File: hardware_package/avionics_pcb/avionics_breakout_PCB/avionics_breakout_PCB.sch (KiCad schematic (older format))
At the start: 15 parts, among them J0 GPS, J1 ANT, J2 SER_1, J3 SER_2, J4 IGN_1, J5 IGN_2, J6 IGN_3, J7 IGN_4, J8 3V3_IN, J9 GND_IN, SW1 SW_Push

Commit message: Finished the new PCB layout for the breakout avionics PCB
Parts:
- Barometer1: symbol avionics_breakout_PCB-rescue:MPL3115A2-Adafruit-avionics -> avionics:MPL3115A2-Adafruit
- IMU1: symbol avionics_breakout_PCB-rescue:MPU-6050-Adafruit-avionics -> avionics:MPU-6050-Adafruit
- LoRa_Radio1: symbol avionics_breakout_PCB-rescue:RFM98-avionics -> avionics:RFM98
- STM32: symbol avionics_breakout_PCB-rescue:Adafruit_Feather_STM32F405-avionics -> avionics:Adafruit_Feather_STM32F405
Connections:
- net +3V3: now also LoRa_Radio1.13 (3V3); no longer LoRa_Radio1.5 (3V3)
- net CS: now also LoRa_Radio1.5 (NSS); no longer LoRa_Radio1.12 (NSS)
- net GND: now also LoRa_Radio1.1 (GND), LoRa_Radio1.10 (GND), LoRa_Radio1.8 (GND); no longer LoRa_Radio1.16 (GND), LoRa_Radio1.2 (GND), LoRa_Radio1.9 (GND)
- net INT_LORA: now also LoRa_Radio1.14 (DIO0); no longer LoRa_Radio1.6 (DIO0)
- net MISO: now also LoRa_Radio1.2 (MISO); no longer LoRa_Radio1.15 (MISO)
- net MOSI: now also LoRa_Radio1.3 (MOSI); no longer LoRa_Radio1.14 (MOSI)
- net RESET: now also LoRa_Radio1.6 (RESET); no longer LoRa_Radio1.11 (RESET)
- net SCK: now also LoRa_Radio1.4 (SCK); no longer LoRa_Radio1.13 (SCK)
- net at J1.1 (Pin_1): now also LoRa_Radio1.9 (ANT); no longer LoRa_Radio1.1 (ANT)
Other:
- moved on the sheet: J1, LoRa_Radio1
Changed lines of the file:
@@
 Text GLabel 6800 1400 0    50   Input ~ 0
 SDA
-Text GLabel 7050 2600 0    50   Input ~ 0
+Text GLabel 7000 2750 0    50   Input ~ 0
 RESET
-Text GLabel 7050 2200 0    50   Input ~ 0
+Text GLabel 7000 2350 0    50   Input ~ 0
 MISO
-Text GLabel 7050 2300 0    50   Input ~ 0
+Text GLabel 7000 2450 0    50   Input ~ 0
 MOSI
-Text GLabel 7050 2400 0    50   Input ~ 0
+Text GLabel 7000 2550 0    50   Input ~ 0
 SCK
-Text GLabel 7050 2500 0    50   Input ~ 0
+Text GLabel 7000 2650 0    50   Input ~ 0
 CS
 Text GLabel 2950 2300 2    50   Input ~ 0
@@
 L power:GND #PWR0102
 U 1 1 5F641D27
-P 6700 3050
-F 0 "#PWR0102" H 6700 2800 50  0001 C CNN
-F 1 "GND" H 6705 2877 50  0000 C CNN
-F 2 "" H 6700 3050 50  0001 C CNN
-F 3 "" H 6700 3050 50  0001 C CNN
-	1    6700 3050
+P 6650 3200
+F 0 "#PWR0102" H 6650 2950 50  0001 C CNN
+F 1 "GND" H 6655 3027 50  0000 C CNN
+F 2 "" H 6650 3200 50  0001 C CNN
+F 3 "" H 6650 3200 50  0001 C CNN
+	1    6650 3200
 	1    0    0    -1
 $EndComp
@@
 	7000 4100 7000 4150
 Wire Wire Line
-	8050 2700 8200 2700
-Wire Wire Line
-	8200 2700 8200 3050
-$Comp
-L avionics_breakout_PCB-rescue:RFM98-avionics LoRa_Radio1
+	8000 2850 8150 2850
+Wire Wire Line
+	8150 2850 8150 3200
+$Comp
+L avionics:RFM98 LoRa_Radio1
 U 1 1 5F636F5E
-P 7550 2450
-F 0 "LoRa_Radio1" H 7550 3065 50  0000 C CNN
-F 1 "RFM98" H 7550 2974 50  0000 C CNN
-F 2 "avionics:RFM98" H 7550 1900 50  0001 C CNN
-F 3 "" H 7550 2450 50  0001 C CNN
-	1    7550 2450
-	1    0    0    -1
-$EndComp
-Wire Wire Line
-	7050 2100 6700 2100
-Wire Wire Line
-	6700 2100 6700 2800
-Wire Wire Line
-	6700 2800 7050 2800
-Connection ~ 6700 2800
-Wire Wire Line
-	6700 2800 6700 3050
-Wire Wire Line
-	8200 3050 6700 3050
-Connection ~ 6700 3050
-$Comp
-L avionics_breakout_PCB-rescue:MPL3115A2-Adafruit-avionics Barometer1
+P 7500 2600
+F 0 "LoRa_Radio1" H 7500 3215 50  0000 C CNN
+F 1 "RFM98" H 7500 3124 50  0000 C CNN
+F 2 "avionics:RFM98" H 7500 2050 50  0001 C CNN
+F 3 "" H 7500 2600 50  0001 C CNN
+	1    7500 2600
+	1    0    0    -1
+$EndComp
+Wire Wire Line
+	7000 2250 6650 2250
+Wire Wire Line
+	6650 2250 6650 2950
+Wire Wire Line
+	6650 2950 7000 2950
+Connection ~ 6650 2950
+Wire Wire Line
+	6650 2950 6650 3200
+Wire Wire Line
+	8150 3200 6650 3200
+Connection ~ 6650 3200
+$Comp
+L avionics:MPL3115A2-Adafruit Barometer1
 U 1 1 5F6344B6
 P 7350 4700
@@
 NoConn ~ 8300 1300
 NoConn ~ 8300 1400
-NoConn ~ 8050 2100
-NoConn ~ 8050 2200
-NoConn ~ 8050 2500
-NoConn ~ 8050 2600
-NoConn ~ 7050 2700
+NoConn ~ 8000 2250
+NoConn ~ 8000 2350
+NoConn ~ 8000 2650
+NoConn ~ 8000 2750
+NoConn ~ 7000 2850
 NoConn ~ 7250 4200
 NoConn ~ 7250 4300
@@
 $EndComp
 $Comp
-L avionics_breakout_PCB-rescue:MPU-6050-Adafruit-avionics IMU1
+L avionics:MPU-6050-Adafruit IMU1
 U 1 1 5F631A9D
 P 7550 1250
@@
 L power:+3.3V #PWR0110
 U 1 1 5F67048B
-P 8600 2400
-F 0 "#PWR0110" H 8600 2250 50  0001 C CNN
-F 1 "+3.3V" H 8615 2573 50  0000 C CNN
-F 2 "" H 8600 2400 50  0001 C CNN
-F 3 "" H 8600 2400 50  0001 C CNN
-	1    8600 2400
-	1    0    0    -1
-$EndComp
-Wire Wire Line
-	8600 2400 8050 2400
+P 8550 2550
+F 0 "#PWR0110" H 8550 2400 50  0001 C CNN
+F 1 "+3.3V" H 8565 2723 50  0000 C CNN
+F 2 "" H 8550 2550 50  0001 C CNN
+F 3 "" H 8550 2550 50  0001 C CNN
+	1    8550 2550
+	1    0    0    -1
+$EndComp
+Wire Wire Line
+	8550 2550 8000 2550
 $Comp
 L power:+3.3V #PWR0111
@@
 L Connector:Conn_01x01_Male J1
 U 1 1 5F636A13
-P 8550 2800
-F 0 "J1" H 8522 2732 50  0000 R CNN
-F 1 "ANT" H 8522 2823 50  0000 R CNN
-F 2 "Connector_Wire:SolderWire-0.1sqmm_1x01_D0.4mm_OD1mm" H 8550 2800 50  0001 C CNN
-F 3 "~" H 8550 2800 50  0001 C CNN
-	1    8550 2800
-	-1   0    0    1
-$EndComp
-Wire Wire Line
-	8050 2800 8350 2800
-Text GLabel 8050 2300 2    50   Input ~ 0
+P 8500 2950
+F 0 "J1" H 8472 2882 50  0000 R CNN
+F 1 "ANT" H 8472 2973 50  0000 R CNN
+F 2 "Connector_Wire:SolderWire-0.1sqmm_1x01_D0.4mm_OD1mm" H 8500 2950 50  0001 C CNN
+F 3 "~" H 8500 2950 50  0001 C CNN
+	1    8500 2950
+	-1   0    0    1
+$EndComp
+Wire Wire Line
+	8000 2950 8300 2950
+Text GLabel 8000 2450 2    50   Input ~ 0
 INT_LORA
 $Comp
-L avionics_breakout_PCB-rescue:Adafruit_Feather_STM32F405-avionics STM32
+L avionics:Adafruit_Feather_STM32F405 STM32
 U 1 1 5F62EEAA
 P 2200 1850
@@
 U 1 1 5F65726D
 P 1100 1700
-F 0 "J3" H 750 1700 50  0000 R CNN
-F 1 "SER_2" H 1050 1700 50  0000 R CNN
+F 0 "J3" H 800 1750 50  0000 R CNN
+F 1 "SER_2" H 1100 1750 50  0000 R CNN
 F 2 "Connector_Wire:SolderWire-0.1sqmm_1x01_D0.4mm_OD1mm" H 1100 1700 50  0001 C CNN
 F 3 "~" H 1100 1700 50  0001 C CNN
@@
 U 1 1 5F658B0B
 P 1100 1800
-F 0 "J2" H 750 1800 50  0000 R CNN
-F 1 "SER_1" H 1050 1800 50  0000 R CNN
+F 0 "J2" H 800 1850 50  0000 R CNN
+F 1 "SER_1" H 1100 1850 50  0000 R CNN
 F 2 "Connector_Wire:SolderWire-0.1sqmm_1x01_D0.4mm_OD1mm" H 1100 1800 50  0001 C CNN
 F 3 "~" H 1100 1800 50  0001 C CNN
@@
 U 1 1 5F65C68E
 P 3250 2100
-F 0 "J4" H 2950 2100 50  0000 R CNN
-F 1 "IGN_1" H 3200 2100 50  0000 R CNN
+F 0 "J4" H 3000 2050 50  0000 R CNN
+F 1 "IGN_1" H 3250 2050 50  0000 R CNN
 F 2 "Connector_Wire:SolderWire-0.1sqmm_1x01_D0.4mm_OD1mm" H 3250 2100 50  0001 C CNN
 F 3 "~" H 3250 2100 50  0001 C CNN
@@
 U 1 1 5F65D9FC
 P 3250 2000
-F 0 "J5" H 2950 2000 50  0000 R CNN
-F 1 "IGN_2" H 3200 2000 50  0000 R CNN
+F 0 "J5" H 3000 1950 50  0000 R CNN
+F 1 "IGN_2" H 3250 1950 50  0000 R CNN
 F 2 "Connector_Wire:SolderWire-0.1sqmm_1x01_D0.4mm_OD1mm" H 3250 2000 50  0001 C CNN
 F 3 "~" H 3250 2000 50  0001 C CNN
@@
 U 1 1 5F65DEA0
 P 3250 1900
-F 0 "J6" H 2950 1900 50  0000 R CNN
-F 1 "IGN_3" H 3200 1900 50  0000 R CNN
+F 0 "J6" H 3000 1850 50  0000 R CNN
+F 1 "IGN_3" H 3250 1850 50  0000 R CNN
 F 2 "Connector_Wire:SolderWire-0.1sqmm_1x01_D0.4mm_OD1mm" H 3250 1900 50  0001 C CNN
 F 3 "~" H 3250 1900 50  0001 C CNN
@@
 U 1 1 5F65E280
 P 3250 1800
-F 0 "J7" H 2950 1800 50  0000 R CNN
-F 1 "IGN_4" H 3200 1800 50  0000 R CNN
+F 0 "J7" H 3000 1750 50  0000 R CNN
+F 1 "IGN_4" H 3250 1750 50  0000 R CNN
 F 2 "Connector_Wire:SolderWire-0.1sqmm_1x01_D0.4mm_OD1mm" H 3250 1800 50  0001 C CNN
 F 3 "~" H 3250 1800 50  0001 C CNN
@@
 U 1 1 5F646CDC
 P 1100 1400
-F 0 "J9" H 750 1400 50  0000 R CNN
-F 1 "GND_IN" H 1050 1400 50  0000 R CNN
+F 0 "J9" H 800 1450 50  0000 R CNN
+F 1 "GND_IN" H 1100 1450 50  0000 R CNN
 F 2 "Connector_Wire:SolderWire-0.1sqmm_1x01_D0.4mm_OD1mm" H 1100 1400 50  0001 C CNN
 F 3 "~" H 1100 1400 50  0001 C CNN
@@
 U 1 1 5F649BF1
 P 1100 1200
-F 0 "J8" H 750 1200 50  0000 R CNN
-F 1 "3V3_IN" H 1050 1200 50  0000 R CNN
+F 0 "J8" H 800 1250 50  0000 R CNN
+F 1 "3V3_IN" H 1100 1250 50  0000 R CNN
 F 2 "Connector_Wire:SolderWire-0.1sqmm_1x01_D0.4mm_OD1mm" H 1100 1200 50  0001 C CNN
 F 3 "~" H 1100 1200 50  0001 C CNN

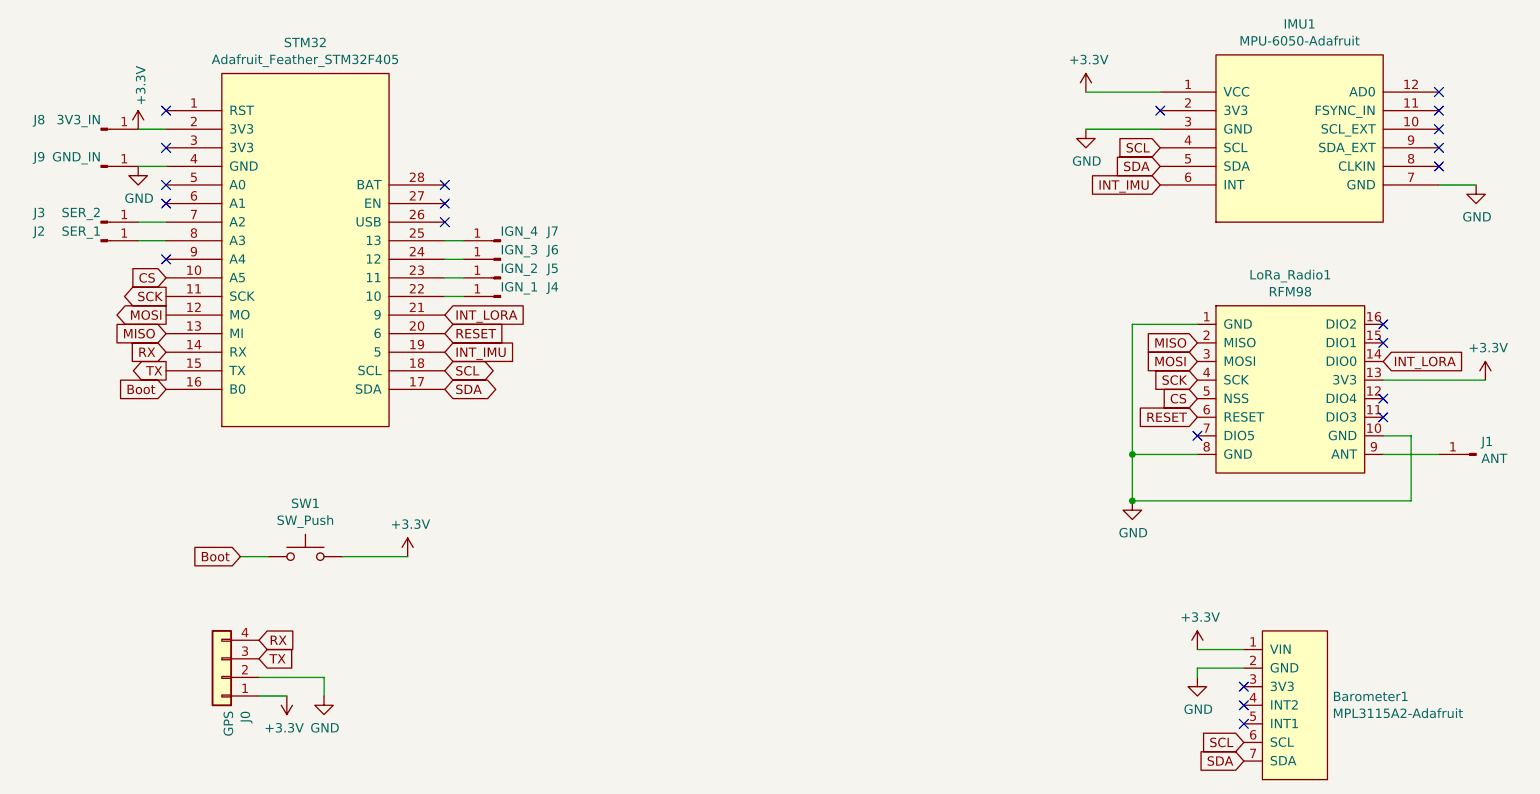
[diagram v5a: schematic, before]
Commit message: Update the avionics breakout PCB and schematic. These updates have made the schematic more readable, and will be used for screenshots within the readme
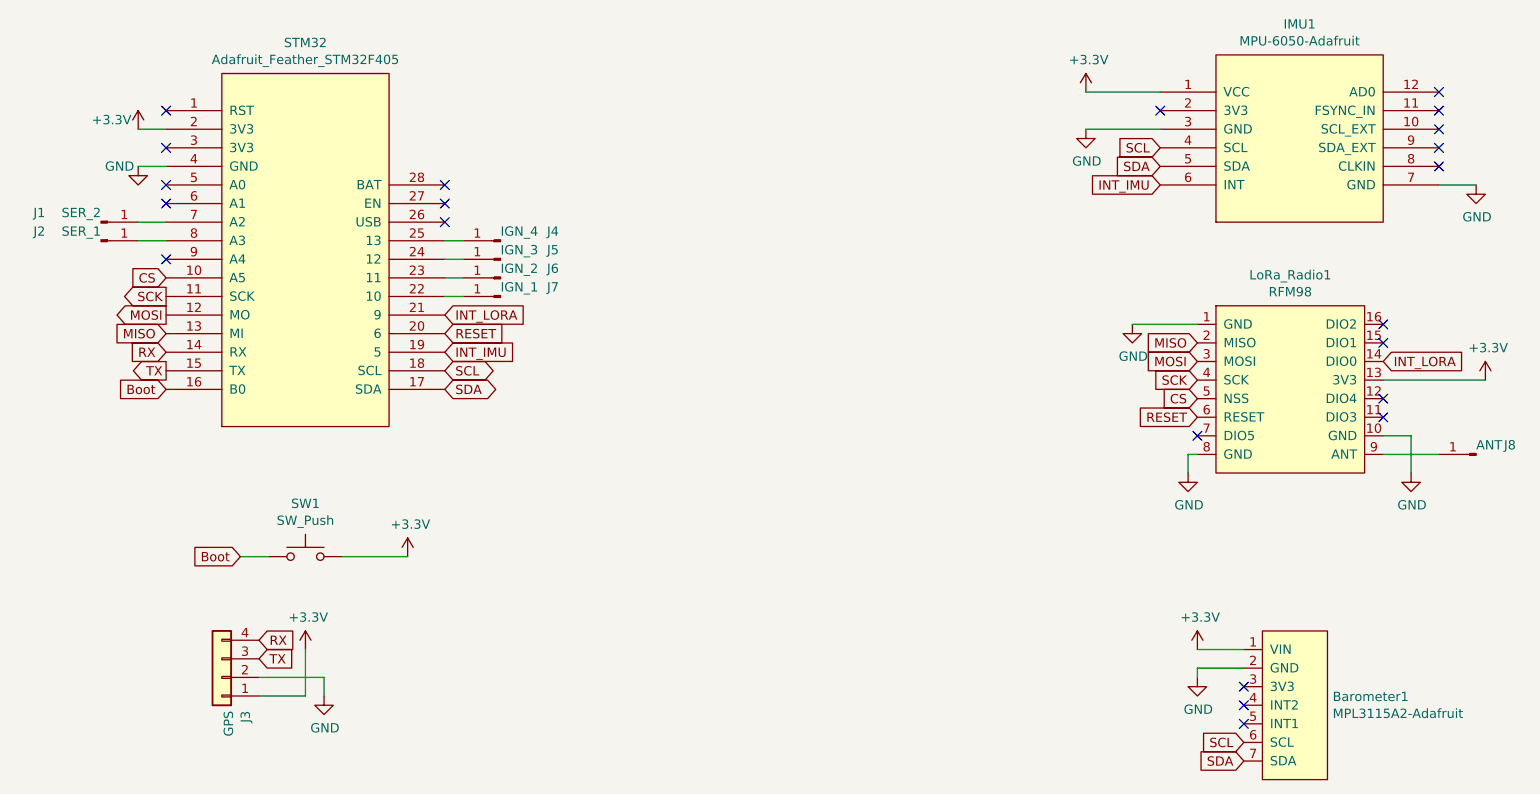
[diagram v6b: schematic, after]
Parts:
- removed J8: 3V3_IN, Connector_Wire:SolderWire-0.1sqmm_1x01_D0.4mm_OD1mm, symbol Connector:Conn_01x01_Male
- removed J9: GND_IN, Connector_Wire:SolderWire-0.1sqmm_1x01_D0.4mm_OD1mm, symbol Connector:Conn_01x01_Male
- renumbered J3 to J1, J0 to J3, J7 to J4, J6 to J5, J5 to J6, J4 to J7, J1 to J8
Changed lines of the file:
@@
 L power:GND #PWR0102
 U 1 1 5F641D27
-P 6650 3200
-F 0 "#PWR0102" H 6650 2950 50  0001 C CNN
-F 1 "GND" H 6655 3027 50  0000 C CNN
-F 2 "" H 6650 3200 50  0001 C CNN
-F 3 "" H 6650 3200 50  0001 C CNN
-	1    6650 3200
+P 8150 3050
+F 0 "#PWR0102" H 8150 2800 50  0001 C CNN
+F 1 "GND" H 8155 2877 50  0000 C CNN
+F 2 "" H 8150 3050 50  0001 C CNN
+F 3 "" H 8150 3050 50  0001 C CNN
+	1    8150 3050
 	1    0    0    -1
 $EndComp
@@
 Wire Wire Line
 	8000 2850 8150 2850
-Wire Wire Line
-	8150 2850 8150 3200
 $Comp
 L avionics:RFM98 LoRa_Radio1
@@
 Wire Wire Line
 	7000 2250 6650 2250
-Wire Wire Line
-	6650 2250 6650 2950
-Wire Wire Line
-	6650 2950 7000 2950
-Connection ~ 6650 2950
-Wire Wire Line
-	6650 2950 6650 3200
-Wire Wire Line
-	8150 3200 6650 3200
-Connection ~ 6650 3200
 $Comp
 L avionics:MPL3115A2-Adafruit Barometer1
@@
 P 1300 1400
 F 0 "#PWR0103" H 1300 1150 50  0001 C CNN
-F 1 "GND" H 1305 1227 50  0000 C CNN
+F 1 "GND" H 1200 1400 50  0000 C CNN
 F 2 "" H 1300 1400 50  0001 C CNN
 F 3 "" H 1300 1400 50  0001 C CNN
@@
 NoConn ~ 2950 1700
 $Comp
-L Connector_Generic:Conn_01x04 J0
+L Connector_Generic:Conn_01x04 J3
 U 1 1 5F64C92F
 P 1750 4150
-F 0 "J0" V 1622 4330 50  0000 L CNN
+F 0 "J3" V 1622 4330 50  0000 L CNN
 F 1 "GPS" V 1713 4330 50  0000 L CNN
 F 2 "Connector_PinHeader_2.54mm:PinHeader_1x04_P2.54mm_Vertical" H 1750 4150 50  0001 C CNN
@@
 P 1300 1200
 F 0 "#PWR0106" H 1300 1050 50  0001 C CNN
-F 1 "+3.3V" V 1315 1328 50  0000 L CNN
+F 1 "+3.3V" H 1050 1250 50  0000 L CNN
 F 2 "" H 1300 1200 50  0001 C CNN
 F 3 "" H 1300 1200 50  0001 C CNN
@@
 L power:+3.3V #PWR0107
 U 1 1 5F661886
-P 2100 4250
-F 0 "#PWR0107" H 2100 4100 50  0001 C CNN
-F 1 "+3.3V" H 2115 4423 50  0000 C CNN
-F 2 "" H 2100 4250 50  0001 C CNN
-F 3 "" H 2100 4250 50  0001 C CNN
-	1    2100 4250
-	-1   0    0    1
+P 2200 4000
+F 0 "#PWR0107" H 2200 3850 50  0001 C CNN
+F 1 "+3.3V" H 2215 4173 50  0000 C CNN
+F 2 "" H 2200 4000 50  0001 C CNN
+F 3 "" H 2200 4000 50  0001 C CNN
+	1    2200 4000
+	1    0    0    -1
 $EndComp
 Wire Wire Line
@@
 Wire Wire Line
 	1950 4150 2300 4150
-Wire Wire Line
-	1950 4250 2100 4250
 $Comp
 L power:+3.3V #PWR0108
@@
 	8500 1500 8300 1500
 $Comp
-L Connector:Conn_01x01_Male J1
+L Connector:Conn_01x01_Male J8
 U 1 1 5F636A13
 P 8500 2950
-F 0 "J1" H 8472 2882 50  0000 R CNN
-F 1 "ANT" H 8472 2973 50  0000 R CNN
+F 0 "J8" H 8350 2900 50  0000 R CNN
+F 1 "ANT" H 8500 2900 50  0000 R CNN
 F 2 "Connector_Wire:SolderWire-0.1sqmm_1x01_D0.4mm_OD1mm" H 8500 2950 50  0001 C CNN
 F 3 "~" H 8500 2950 50  0001 C CNN
@@
 $EndComp
 $Comp
-L Connector:Conn_01x01_Male J3
+L Connector:Conn_01x01_Male J1
 U 1 1 5F65726D
 P 1100 1700
-F 0 "J3" H 800 1750 50  0000 R CNN
+F 0 "J1" H 800 1750 50  0000 R CNN
 F 1 "SER_2" H 1100 1750 50  0000 R CNN
 F 2 "Connector_Wire:SolderWire-0.1sqmm_1x01_D0.4mm_OD1mm" H 1100 1700 50  0001 C CNN
@@
 	1300 1800 1450 1800
 $Comp
-L Connector:Conn_01x01_Male J4
+L Connector:Conn_01x01_Male J7
 U 1 1 5F65C68E
 P 3250 2100
-F 0 "J4" H 3000 2050 50  0000 R CNN
+F 0 "J7" H 3000 2050 50  0000 R CNN
 F 1 "IGN_1" H 3250 2050 50  0000 R CNN
 F 2 "Connector_Wire:SolderWire-0.1sqmm_1x01_D0.4mm_OD1mm" H 3250 2100 50  0001 C CNN
@@
 $EndComp
 $Comp
-L Connector:Conn_01x01_Male J5
+L Connector:Conn_01x01_Male J6
 U 1 1 5F65D9FC
 P 3250 2000
-F 0 "J5" H 3000 1950 50  0000 R CNN
+F 0 "J6" H 3000 1950 50  0000 R CNN
 F 1 "IGN_2" H 3250 1950 50  0000 R CNN
 F 2 "Connector_Wire:SolderWire-0.1sqmm_1x01_D0.4mm_OD1mm" H 3250 2000 50  0001 C CNN
@@
 $EndComp
 $Comp
-L Connector:Conn_01x01_Male J6
+L Connector:Conn_01x01_Male J5
 U 1 1 5F65DEA0
 P 3250 1900
-F 0 "J6" H 3000 1850 50  0000 R CNN
+F 0 "J5" H 3000 1850 50  0000 R CNN
 F 1 "IGN_3" H 3250 1850 50  0000 R CNN
 F 2 "Connector_Wire:SolderWire-0.1sqmm_1x01_D0.4mm_OD1mm" H 3250 1900 50  0001 C CNN
@@
 $EndComp
 $Comp
-L Connector:Conn_01x01_Male J7
+L Connector:Conn_01x01_Male J4
 U 1 1 5F65E280
 P 3250 1800
-F 0 "J7" H 3000 1750 50  0000 R CNN
+F 0 "J4" H 3000 1750 50  0000 R CNN
 F 1 "IGN_4" H 3250 1750 50  0000 R CNN
 F 2 "Connector_Wire:SolderWire-0.1sqmm_1x01_D0.4mm_OD1mm" H 3250 1800 50  0001 C CNN
@@
 Wire Wire Line
 	2950 2100 3050 2100
-$Comp
-L Connector:Conn_01x01_Male J9
-U 1 1 5F646CDC
-P 1100 1400
-F 0 "J9" H 800 1450 50  0000 R CNN
-F 1 "GND_IN" H 1100 1450 50  0000 R CNN
-F 2 "Connector_Wire:SolderWire-0.1sqmm_1x01_D0.4mm_OD1mm" H 1100 1400 50  0001 C CNN
-F 3 "~" H 1100 1400 50  0001 C CNN
-	1    1100 1400
-	1    0    0    -1
-$EndComp
-$Comp
-L Connector:Conn_01x01_Male J8
-U 1 1 5F649BF1
-P 1100 1200
-F 0 "J8" H 800 1250 50  0000 R CNN
-F 1 "3V3_IN" H 1100 1250 50  0000 R CNN
-F 2 "Connector_Wire:SolderWire-0.1sqmm_1x01_D0.4mm_OD1mm" H 1100 1200 50  0001 C CNN
-F 3 "~" H 1100 1200 50  0001 C CNN
-	1    1100 1200
-	1    0    0    -1
-$EndComp
 NoConn ~ 1450 1300
+Wire Wire Line
+	2200 4000 2200 4250
+Wire Wire Line
+	1950 4250 2200 4250
+$Comp
+L power:GND #PWR0113
+U 1 1 5F74C44E
+P 6950 3050
+F 0 "#PWR0113" H 6950 2800 50  0001 C CNN
+F 1 "GND" H 6955 2877 50  0000 C CNN
+F 2 "" H 6950 3050 50  0001 C CNN
+F 3 "" H 6950 3050 50  0001 C CNN
+	1    6950 3050
+	1    0    0    -1
+$EndComp
+Wire Wire Line
+	7000 2950 6950 2950
+Wire Wire Line
+	6950 2950 6950 3050
+Wire Wire Line
+	8150 2850 8150 3050
+$Comp
+L power:GND #PWR0114
+U 1 1 5F74F62C
+P 6650 2250
+F 0 "#PWR0114" H 6650 2000 50  0001 C CNN
+F 1 "GND" H 6655 2077 50  0000 C CNN
+F 2 "" H 6650 2250 50  0001 C CNN
+F 3 "" H 6650 2250 50  0001 C CNN
+	1    6650 2250
+	1    0    0    -1
+$EndComp
 $EndSCHEMATC
